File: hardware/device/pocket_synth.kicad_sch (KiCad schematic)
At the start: 19 parts, among them SW24 NRST, U18 STM32H743ZIT6

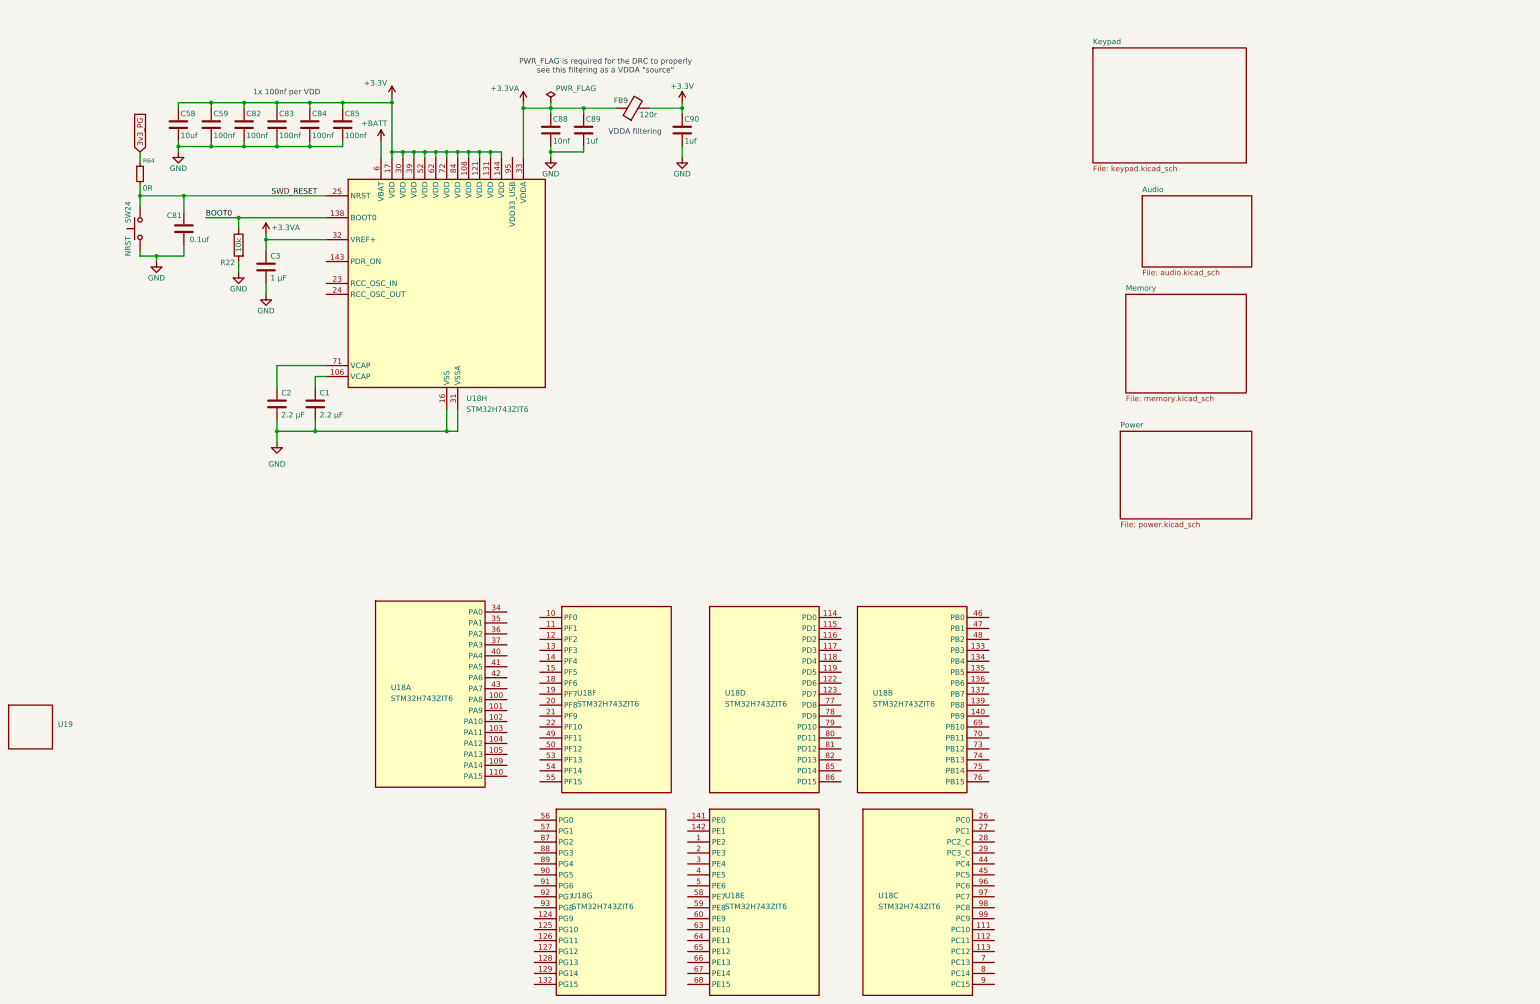
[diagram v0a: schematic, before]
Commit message: feat: various footprint updates, 3d models, tollerances
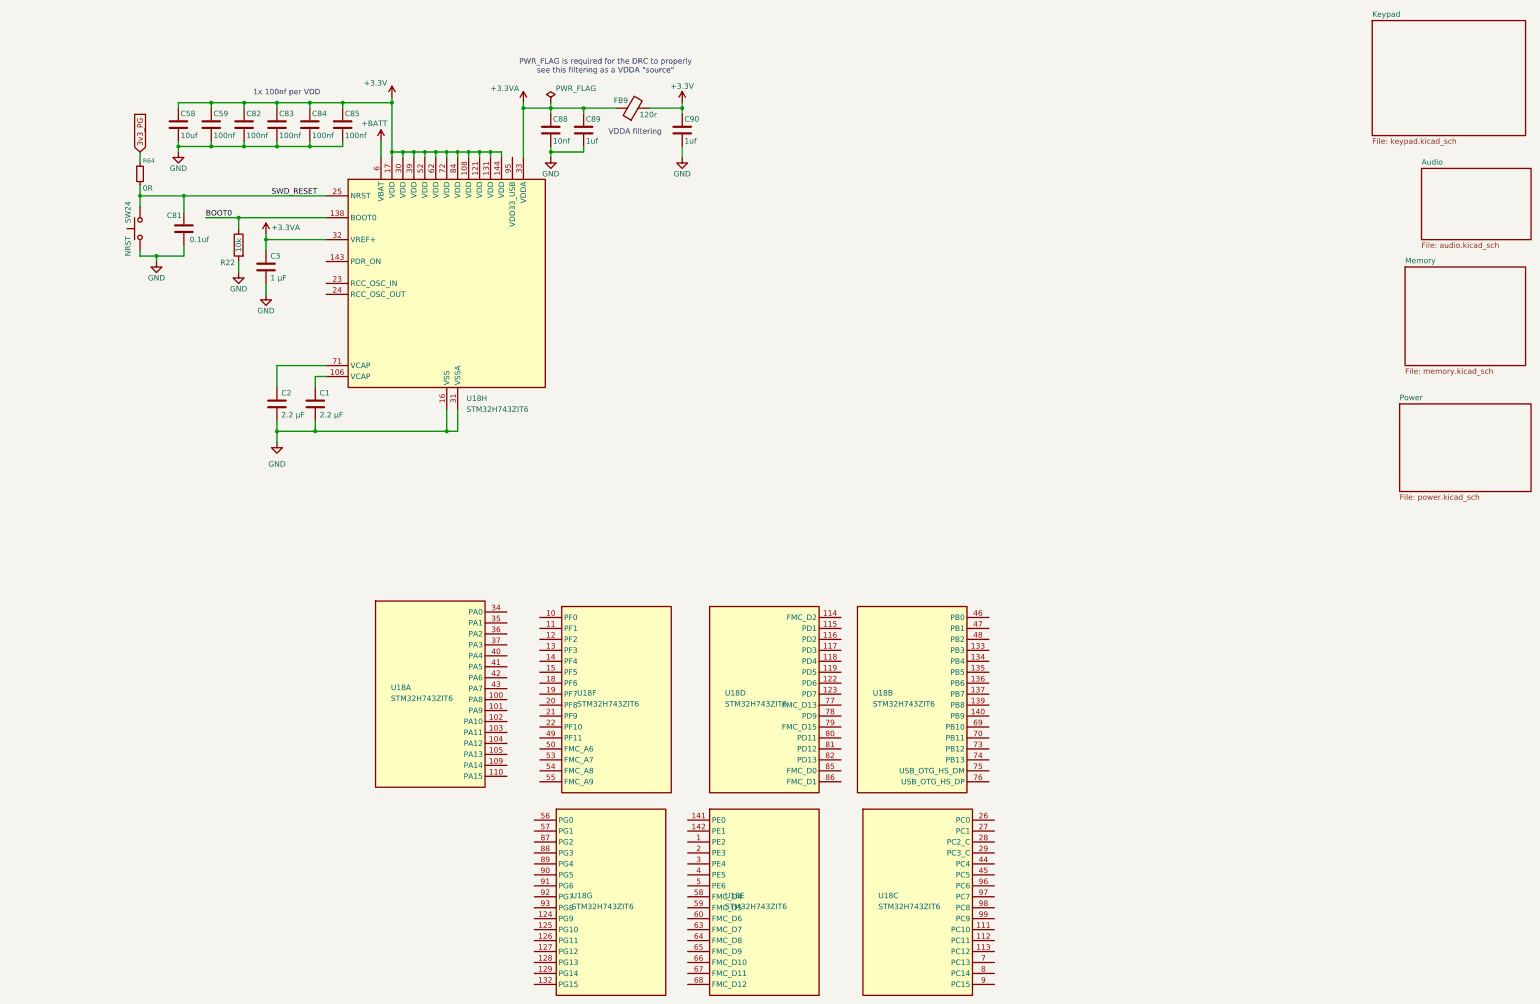
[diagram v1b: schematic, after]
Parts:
- removed U19: ~, pocket_synth:ER-TFT024IPS-3, symbol pocket_synth:ER-TFT024IPS-3
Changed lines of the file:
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@@
 	)
 	(symbol
-		(lib_id "pocket_synth:ER-TFT024IPS-3")
-		(at -3.81 172.72 0)
-		(unit 1)
-		(exclude_from_sim no)
-		(in_bom yes)
-		(on_board yes)
-		(dnp no)
-		(fields_autoplaced yes)
-		(property "Reference" "U19"
-			(at 2.54 172.0849 0)
-			(effects
-				(font
-					(size 1.27 1.27)
-				)
-				(justify left)
-			)
-		)
-		(property "Value" "~"
-			(at 2.54 173.99 0)
-			(effects
-				(font
-					(size 1.27 1.27)
-				)
-				(justify left)
-			)
-		)
-		(property "Footprint" "pocket_synth:ER-TFT024IPS-3"
-			(at -3.81 172.72 0)
-			(effects
-				(font
-					(size 1.27 1.27)
-				)
-				(hide yes)
-			)
-		)
-		(property "Datasheet" ""
-			(at -3.81 172.72 0)
-			(effects
-				(font
-					(size 1.27 1.27)
-				)
-				(hide yes)
-			)
-		)
-		(property "Description" ""
-			(at -3.81 172.72 0)
-			(effects
-				(font
-					(size 1.27 1.27)
-				)
-				(hide yes)
-			)
-		)
-		(property "JLC" ""
-			(at -3.81 172.72 0)
-			(effects
-				(font
-					(size 1.27 1.27)
-				)
-			)
-		)
-		(instances
-			(project ""
-				(path "/485383b8-00f4-4405-b270-de249939cff4"
-					(reference "U19")
-					(unit 1)
-				)
-			)
-		)
-	)
-	(symbol
 		(lib_id "Switch:SW_Push")
 		(at 21.59 57.15 90)
@@
 		)
 		(pin "114"
+			(alternate "FMC_D2")
 		)
 		(pin "115"
@@
 		)
 		(pin "77"
+			(alternate "FMC_D13")
 		)
 		(pin "78"
 		)
 		(pin "79"
+			(alternate "FMC_D15")
 		)
 		(pin "80"
@@
 		)
 		(pin "85"
+			(alternate "FMC_D0")
 		)
 		(pin "86"
+			(alternate "FMC_D1")
 		)
 		(pin "94"
@@
 		)
 		(pin "63"
+			(alternate "FMC_D7")
 		)
 		(pin "6"
@@
 		)
 		(pin "65"
+			(alternate "FMC_D9")
 		)
 		(pin "17"
@@
 		)
 		(pin "60"
+			(alternate "FMC_D6")
 		)
 		(pin "67"
+			(alternate "FMC_D11")
 		)
 		(pin "68"
+			(alternate "FMC_D12")
 		)
 		(pin "90"
@@
 		)
 		(pin "64"
+			(alternate "FMC_D8")
 		)
 		(pin "20"
@@
 		)
 		(pin "59"
+			(alternate "FMC_D5")
 		)
 		(pin "87"
@@
 		)
 		(pin "58"
+			(alternate "FMC_D4")
 		)
 		(pin "49"
@@
 		)
 		(pin "66"
+			(alternate "FMC_D10")
 		)
 		(pin "143"
@@
 		)
 		(pin "50"
+			(alternate "FMC_A6")
 		)
 		(pin "5"
@@
 		)
 		(pin "54"
+			(alternate "FMC_A8")
 		)
 		(pin "53"
+			(alternate "FMC_A7")
 		)
 		(pin "125"
@@
 		)
 		(pin "55"
+			(alternate "FMC_A9")
 		)
 		(pin "56"
@@
 		)
 		(pin "76"
+			(alternate "USB_OTG_HS_DP")
 		)
 		(pin "26"
@@
 		)
 		(pin "75"
+			(alternate "USB_OTG_HS_DM")
 		)
 		(pin "55"
@@
 	)
 	(sheet
-		(at 248.92 104.14)
+		(at 313.69 97.79)
 		(size 30.48 20.32)
 		(exclude_from_sim no)
@@
 		)
 		(property "Sheetname" "Power"
-			(at 248.92 103.4284 0)
+			(at 313.69 97.0784 0)
 			(effects
 				(font
@@
 		)
 		(property "Sheetfile" "power.kicad_sch"
-			(at 248.92 125.0446 0)
+			(at 313.69 118.6946 0)
 			(effects
 				(font
@@
 	)
 	(sheet
-		(at 242.57 15.24)
+		(at 307.34 8.89)
 		(size 35.56 26.67)
 		(exclude_from_sim no)
@@
 		)
 		(property "Sheetname" "Keypad"
-			(at 242.57 14.5284 0)
+			(at 307.34 8.1784 0)
 			(effects
 				(font
@@
 		)
 		(property "Sheetfile" "keypad.kicad_sch"
-			(at 242.57 42.4946 0)
+			(at 307.34 36.1446 0)
 			(effects
 				(font
@@
 	)
 	(sheet
-		(at 254 49.53)
+		(at 318.77 43.18)
 		(size 25.4 16.51)
 		(exclude_from_sim no)
@@
 		)
 		(property "Sheetname" "Audio"
-			(at 254 48.8184 0)
+			(at 318.77 42.4684 0)
 			(effects
 				(font
@@
 		)
 		(property "Sheetfile" "audio.kicad_sch"
-			(at 254 66.6246 0)
+			(at 318.77 60.2746 0)
 			(effects
 				(font
@@
 	)
 	(sheet
-		(at 250.19 72.39)
+		(at 314.96 66.04)
 		(size 27.94 22.86)
 		(exclude_from_sim no)
@@
 		)
 		(property "Sheetname" "Memory"
-			(at 250.19 71.6784 0)
+			(at 314.96 65.3284 0)
 			(effects
 				(font
@@
 		)
 		(property "Sheetfile" "memory.kicad_sch"
-			(at 250.19 95.8346 0)
+			(at 314.96 89.4846 0)
 			(effects
 				(font

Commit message: feat: audio schematic, FMC bus, SDRAM connections
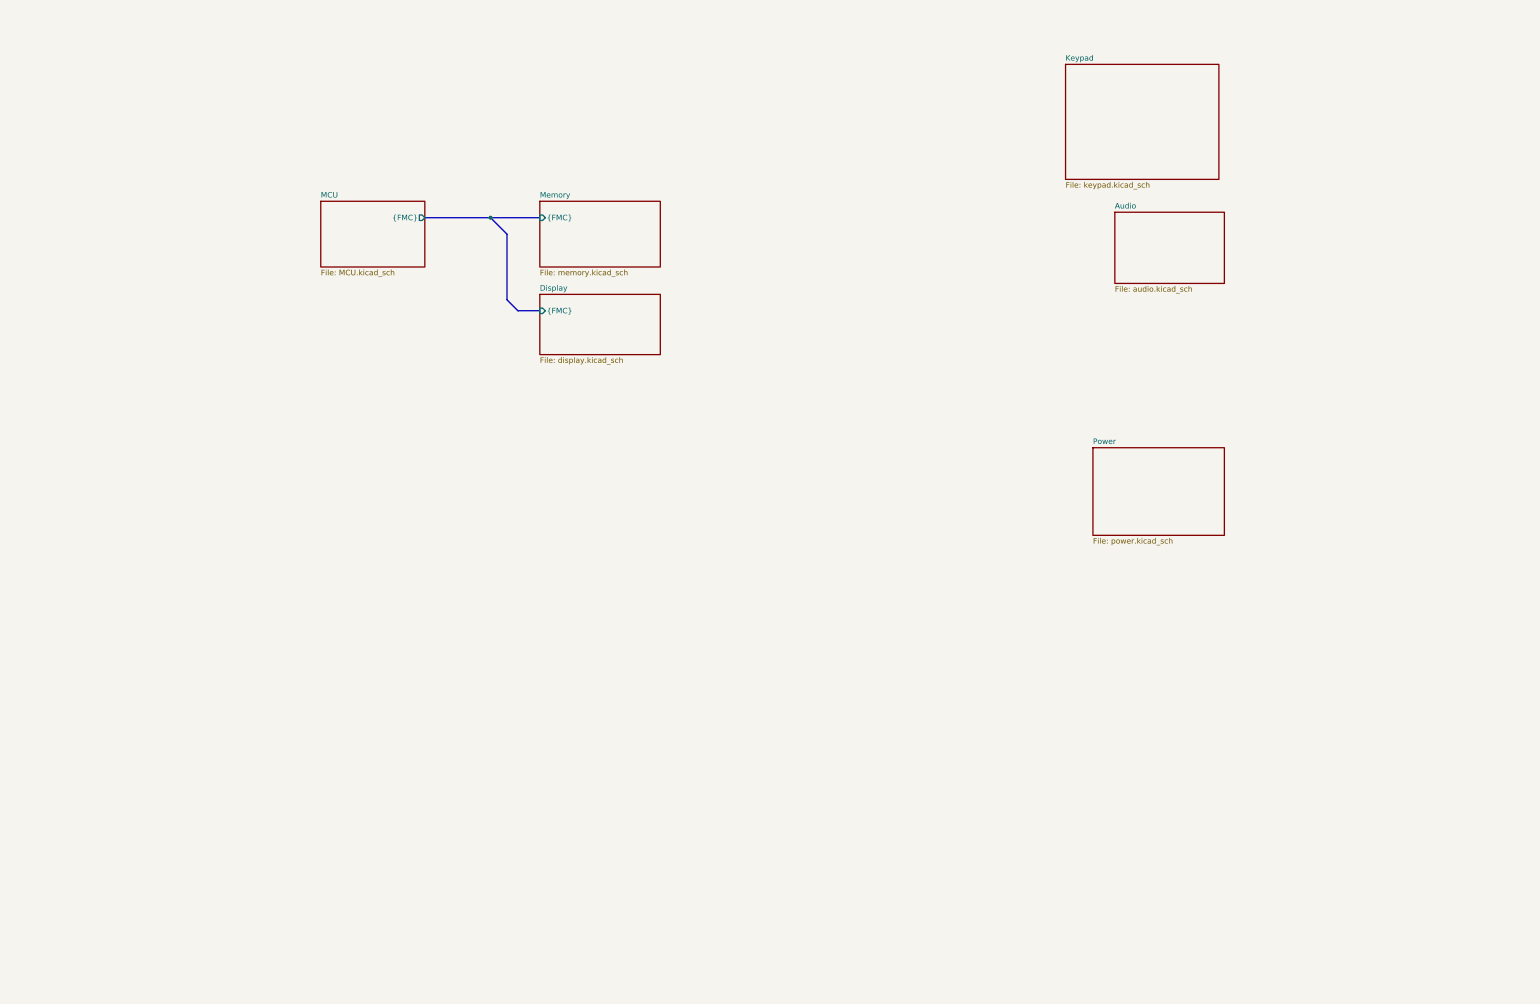
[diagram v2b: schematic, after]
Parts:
- removed C1, C2: 2.2 µF, Capacitor_SMD:C_0603_1608Metric_Pad1.08x0.95mm_HandSolder, symbol Device:C
- removed C3: 1 µF, Capacitor_SMD:C_0603_1608Metric_Pad1.08x0.95mm_HandSolder, symbol Device:C
- removed C58: 10uf, Capacitor_SMD:C_0603_1608Metric_Pad1.08x0.95mm_HandSolder, symbol Device:C
- removed C59, C82, C83, C84, C85: 100nf, Capacitor_SMD:C_0603_1608Metric_Pad1.08x0.95mm_HandSolder, symbol Device:C
- removed C81: 0.1uf, Capacitor_SMD:C_0603_1608Metric_Pad1.08x0.95mm_HandSolder, symbol Device:C
- removed C88: 10nf, Capacitor_SMD:C_0603_1608Metric_Pad1.08x0.95mm_HandSolder, symbol Device:C
- removed C89, C90: 1uf, Capacitor_SMD:C_0603_1608Metric_Pad1.08x0.95mm_HandSolder, symbol Device:C
- removed FB9: 120r, symbol Device:FerriteBead
- removed R22: 10k, Resistor_SMD:R_0201_0603Metric_Pad0.64x0.40mm_HandSolder, symbol Device:R
- removed R64: 0R, Resistor_SMD:R_0201_0603Metric_Pad0.64x0.40mm_HandSolder, symbol Device:R_Small
- removed SW24: NRST, symbol Switch:SW_Push
- removed U18: STM32H743ZIT6, Package_QFP:LQFP-144_20x20mm_P0.5mm, symbol MCU_ST_STM32H7:STM32H743ZITx
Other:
- added sheet Display (display.kicad_sch)
- added sheet MCU (MCU.kicad_sch)
- sheet Memory ports: added {FMC}; removed none
- note removed: "1x 100nf per VDD"
- note removed: "PWR_FLAG is required for the DRC to properly see this filtering as a VDDA "source""
- note removed: "VDDA filtering"
